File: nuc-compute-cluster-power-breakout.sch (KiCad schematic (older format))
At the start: 9 parts, among them J2 BM04B-SRSS-TB-LF-SN, J3 BM04B-SRSS-TB-LF-SN, J5 430450812, J6 430450812, J7 430450812, J8 430450812, J9 430450812

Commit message: Loclib update
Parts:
- J2, J3: footprint antmicro-footprints:BM04B-SRSS-TB-LF-SN -> nuc-compute-cluster-power-breakout-footprints:BM04B-SRSS-TB-LF-SN; symbol antmicroRectangularConnectorsHeadersMalePins:BM04B-SRSS-TB-LF-SN -> nuc-compute-cluster-power-breakout:BM04B-SRSS-TB-LF-SN
- J5, J6, J7, J8, J9: footprint antmicro-footprints:Molex-43045-0812 -> nuc-compute-cluster-power-breakout-footprints:Molex-43045-0812; symbol antmicroRectangularConnectorsHeadersFemalePins:430450812 -> nuc-compute-cluster-power-breakout:430450812
- R10, R9: footprint antmicro-footprints:0402-res -> nuc-compute-cluster-power-breakout-footprints:0402-res; symbol antmicroResistors0402:R_0R_0402 -> nuc-compute-cluster-power-breakout:R_0R_0402
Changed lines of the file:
@@
 $EndSheet
 $Comp
-L antmicroRectangularConnectorsHeadersMalePins:BM04B-SRSS-TB-LF-SN J2
+L nuc-compute-cluster-power-breakout:BM04B-SRSS-TB-LF-SN J2
 U 1 1 6231F410
 P 2150 2150
 F 0 "J2" H 2100 2500 50  0000 L CNN
 F 1 "BM04B-SRSS-TB-LF-SN" H 2000 2000 50  0000 L CNN
-F 2 "antmicro-footprints:BM04B-SRSS-TB-LF-SN" H 2150 1900 50  0001 C CNN
+F 2 "nuc-compute-cluster-power-breakout-footprints:BM04B-SRSS-TB-LF-SN" H 2150 1900 50  0001 C CNN
 F 3 "https://www.jst-mfg.com/product/pdf/eng/eSH.pdf" H 1700 1850 50  0001 C CNN
 F 4 "BM04B-SRSS-TB(LF)(SN) " H 2050 1800 50  0001 L CNN "MPN"
@@
 $EndComp
 $Comp
-L antmicroRectangularConnectorsHeadersMalePins:BM04B-SRSS-TB-LF-SN J3
+L nuc-compute-cluster-power-breakout:BM04B-SRSS-TB-LF-SN J3
 U 1 1 6231FA57
 P 3900 2150
 F 0 "J3" H 3850 2500 50  0000 L CNN
 F 1 "BM04B-SRSS-TB-LF-SN" H 3750 2000 50  0000 L CNN
-F 2 "antmicro-footprints:BM04B-SRSS-TB-LF-SN" H 3900 1900 50  0001 C CNN
+F 2 "nuc-compute-cluster-power-breakout-footprints:BM04B-SRSS-TB-LF-SN" H 3900 1900 50  0001 C CNN
 F 3 "https://www.jst-mfg.com/product/pdf/eng/eSH.pdf" H 3450 1850 50  0001 C CNN
 F 4 "BM04B-SRSS-TB(LF)(SN) " H 3800 1800 50  0001 L CNN "MPN"
@@
 $EndComp
 $Comp
-L power:GND #PWR023
+L nuc-compute-cluster-power-breakout:GND #PWR023
 U 1 1 6232221D
 P 1800 2300
@@
 	1800 2200 1950 2200
 $Comp
-L power:GND #PWR033
+L nuc-compute-cluster-power-breakout:GND #PWR033
 U 1 1 62322D69
 P 3550 2300
@@
 VCC3V3
 $Comp
-L antmicroResistors0402:R_0R_0402 R9
+L nuc-compute-cluster-power-breakout:R_0R_0402 R9
 U 1 1 62328EB6
 P 1800 1600
 F 0 "R9" V 1755 1670 60  0000 L CNN
 F 1 "R_0R_0402" H 1800 1450 60  0001 C CNN
-F 2 "antmicro-footprints:0402-res" H 2000 1800 60  0001 L CNN
+F 2 "nuc-compute-cluster-power-breakout-footprints:0402-res" H 2000 1800 60  0001 L CNN
 F 3 "" H 1800 1600 50  0001 C CNN
 F 4 "PANASONIC" H 2000 2000 60  0001 L CNN "Manufacturer"
@@
 $EndComp
 $Comp
-L antmicroResistors0402:R_0R_0402 R10
+L nuc-compute-cluster-power-breakout:R_0R_0402 R10
 U 1 1 62329827
 P 3550 1600
 F 0 "R10" V 3505 1670 60  0000 L CNN
 F 1 "R_0R_0402" H 3550 1450 60  0001 C CNN
-F 2 "antmicro-footprints:0402-res" H 3750 1800 60  0001 L CNN
+F 2 "nuc-compute-cluster-power-breakout-footprints:0402-res" H 3750 1800 60  0001 L CNN
 F 3 "" H 3550 1600 50  0001 C CNN
 F 4 "PANASONIC" H 3750 2000 60  0001 L CNN "Manufacturer"
@@
 $EndBitmap
 $Comp
-L antmicroRectangularConnectorsHeadersFemalePins:430450812 J5
+L nuc-compute-cluster-power-breakout:430450812 J5
 U 1 1 62389198
 P 2100 3300
 F 0 "J5" H 2125 3565 50  0000 C CNN
 F 1 "430450812" H 2125 3474 50  0000 C CNN
-F 2 "antmicro-footprints:Molex-43045-0812" H 1950 3300 50  0001 C CNN
+F 2 "nuc-compute-cluster-power-breakout-footprints:Molex-43045-0812" H 1950 3300 50  0001 C CNN
 F 3 "https://www.molex.com/pdm_docs/sd/430450812_sd.pdf" H 1950 3300 50  0001 C CNN
 F 4 "430450812" H 2100 3300 50  0001 C CNN "MPN"
@@
 $EndComp
 $Comp
-L antmicroRectangularConnectorsHeadersFemalePins:430450812 J6
+L nuc-compute-cluster-power-breakout:430450812 J6
 U 1 1 623895A5
 P 3650 3300
 F 0 "J6" H 3675 3565 50  0000 C CNN
 F 1 "430450812" H 3675 3474 50  0000 C CNN
-F 2 "antmicro-footprints:Molex-43045-0812" H 3500 3300 50  0001 C CNN
+F 2 "nuc-compute-cluster-power-breakout-footprints:Molex-43045-0812" H 3500 3300 50  0001 C CNN
 F 3 "https://www.molex.com/pdm_docs/sd/430450812_sd.pdf" H 3500 3300 50  0001 C CNN
 F 4 "430450812" H 3650 3300 50  0001 C CNN "MPN"
@@
 $EndComp
 $Comp
-L antmicroRectangularConnectorsHeadersFemalePins:430450812 J7
+L nuc-compute-cluster-power-breakout:430450812 J7
 U 1 1 6238989A
 P 2100 4250
 F 0 "J7" H 2125 4515 50  0000 C CNN
 F 1 "430450812" H 2125 4424 50  0000 C CNN
-F 2 "antmicro-footprints:Molex-43045-0812" H 1950 4250 50  0001 C CNN
+F 2 "nuc-compute-cluster-power-breakout-footprints:Molex-43045-0812" H 1950 4250 50  0001 C CNN
 F 3 "https://www.molex.com/pdm_docs/sd/430450812_sd.pdf" H 1950 4250 50  0001 C CNN
 F 4 "430450812" H 2100 4250 50  0001 C CNN "MPN"
@@
 $EndComp
 $Comp
-L antmicroRectangularConnectorsHeadersFemalePins:430450812 J8
+L nuc-compute-cluster-power-breakout:430450812 J8
 U 1 1 62389AA4
 P 3650 4250
 F 0 "J8" H 3675 4515 50  0000 C CNN
 F 1 "430450812" H 3675 4424 50  0000 C CNN
-F 2 "antmicro-footprints:Molex-43045-0812" H 3500 4250 50  0001 C CNN
+F 2 "nuc-compute-cluster-power-breakout-footprints:Molex-43045-0812" H 3500 4250 50  0001 C CNN
 F 3 "https://www.molex.com/pdm_docs/sd/430450812_sd.pdf" H 3500 4250 50  0001 C CNN
 F 4 "430450812" H 3650 4250 50  0001 C CNN "MPN"
@@
 $EndComp
 $Comp
-L antmicroRectangularConnectorsHeadersFemalePins:430450812 J9
+L nuc-compute-cluster-power-breakout:430450812 J9
 U 1 1 62389CDB
 P 2850 5400
 F 0 "J9" H 2875 5665 50  0000 C CNN
 F 1 "430450812" H 2875 5574 50  0000 C CNN
-F 2 "antmicro-footprints:Molex-43045-0812" H 2700 5400 50  0001 C CNN
+F 2 "nuc-compute-cluster-power-breakout-footprints:Molex-43045-0812" H 2700 5400 50  0001 C CNN
 F 3 "https://www.molex.com/pdm_docs/sd/430450812_sd.pdf" H 2700 5400 50  0001 C CNN
 F 4 "430450812" H 2850 5400 50  0001 C CNN "MPN"
@@
 	1750 3450 1750 3400
 $Comp
-L power:GND #PWR027
+L nuc-compute-cluster-power-breakout:GND #PWR027
 U 1 1 62392E27
 P 2400 3750
@@
 	2400 3600 2400 3500
 $Comp
-L power:GND #PWR030
+L nuc-compute-cluster-power-breakout:GND #PWR030
 U 1 1 62394589
 P 2400 4800
@@
 	2400 4550 2400 4450
 $Comp
-L power:GND #PWR035
+L nuc-compute-cluster-power-breakout:GND #PWR035
 U 1 1 6239614B
 P 3950 4800
@@
 	3950 4550 3950 4450
 $Comp
-L power:GND #PWR031
+L nuc-compute-cluster-power-breakout:GND #PWR031
 U 1 1 62398F4B
 P 3150 6000
@@
 	3150 5700 3150 5600
 $Comp
-L power:GND #PWR034
+L nuc-compute-cluster-power-breakout:GND #PWR034
 U 1 1 62399AC9
 P 3950 3750

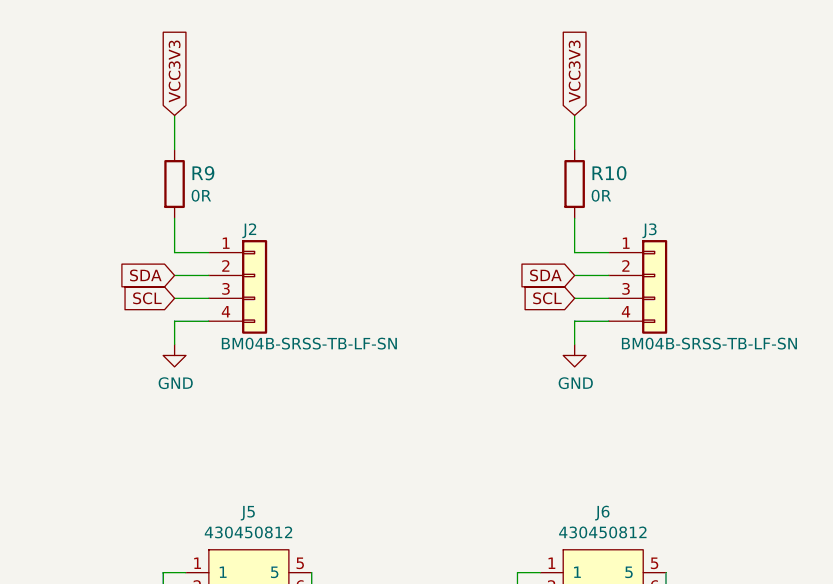
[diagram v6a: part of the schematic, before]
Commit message: Add remarks on the schematic sheets
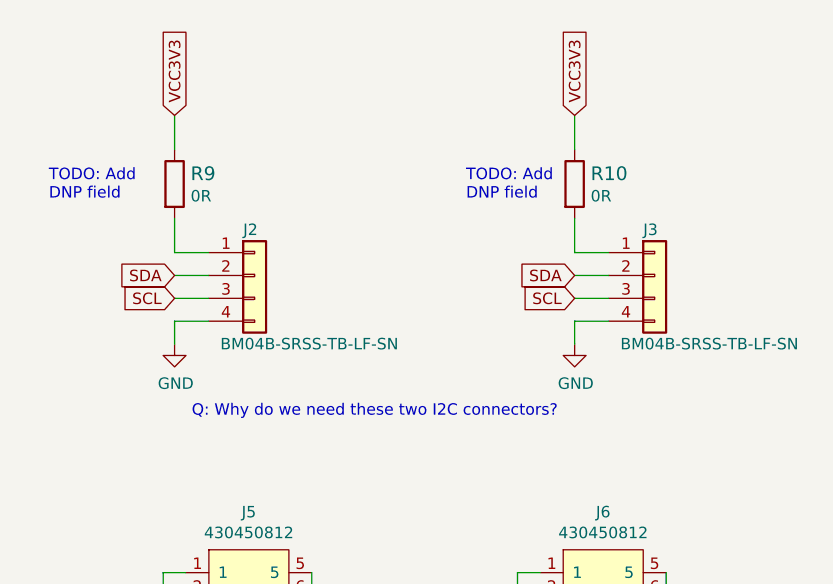
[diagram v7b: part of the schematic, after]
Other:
- note added: "Q: Why do we need these two I2C connectors?"
- note added: "TODO: Add \nDNP field"
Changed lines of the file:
@@
 Wire Wire Line
 	3300 4400 3300 4450
+Text Notes 1250 1675 0    50   ~ 0
+TODO: Add \nDNP field
+Text Notes 3075 1675 0    50   ~ 0
+TODO: Add \nDNP field
+Text Notes 1875 2625 0    50   ~ 0
+Q: Why do we need these two I2C connectors?
 $EndSCHEMATC

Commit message: Improvements after review
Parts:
- R10, R9: DNP (none) -> DNP
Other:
- note removed: "TODO: Add \nDNP field"
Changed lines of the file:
@@
 F 5 "ERJ2GE0R00X" H 2000 1900 60  0001 L CNN "MPN"
 F 6 "0R" V 1853 1670 50  0000 L CNN "Val"
+F 7 "DNP" H 1800 1600 50  0000 C CNN "DNP"
 	1    1800 1600
 	0    1    1    0
@@
 F 5 "ERJ2GE0R00X" H 3750 1900 60  0001 L CNN "MPN"
 F 6 "0R" V 3603 1670 50  0000 L CNN "Val"
+F 7 "DNP" H 3550 1600 50  0000 C CNN "DNP"
 	1    3550 1600
 	0    1    1    0
@@
 Wire Wire Line
 	3300 4400 3300 4450
-Text Notes 1250 1675 0    50   ~ 0
-TODO: Add \nDNP field
-Text Notes 3075 1675 0    50   ~ 0
-TODO: Add \nDNP field
 Text Notes 1875 2625 0    50   ~ 0
 Q: Why do we need these two I2C connectors?
